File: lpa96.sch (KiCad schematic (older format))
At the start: 26 parts, among them IC1 ATMEGA328-A, P1 CONN_2, P2 CONN_3X2, SW1 SW_PUSH, U1 SD_CARD, U2 LD1117S33, Y1 RESONATEUR

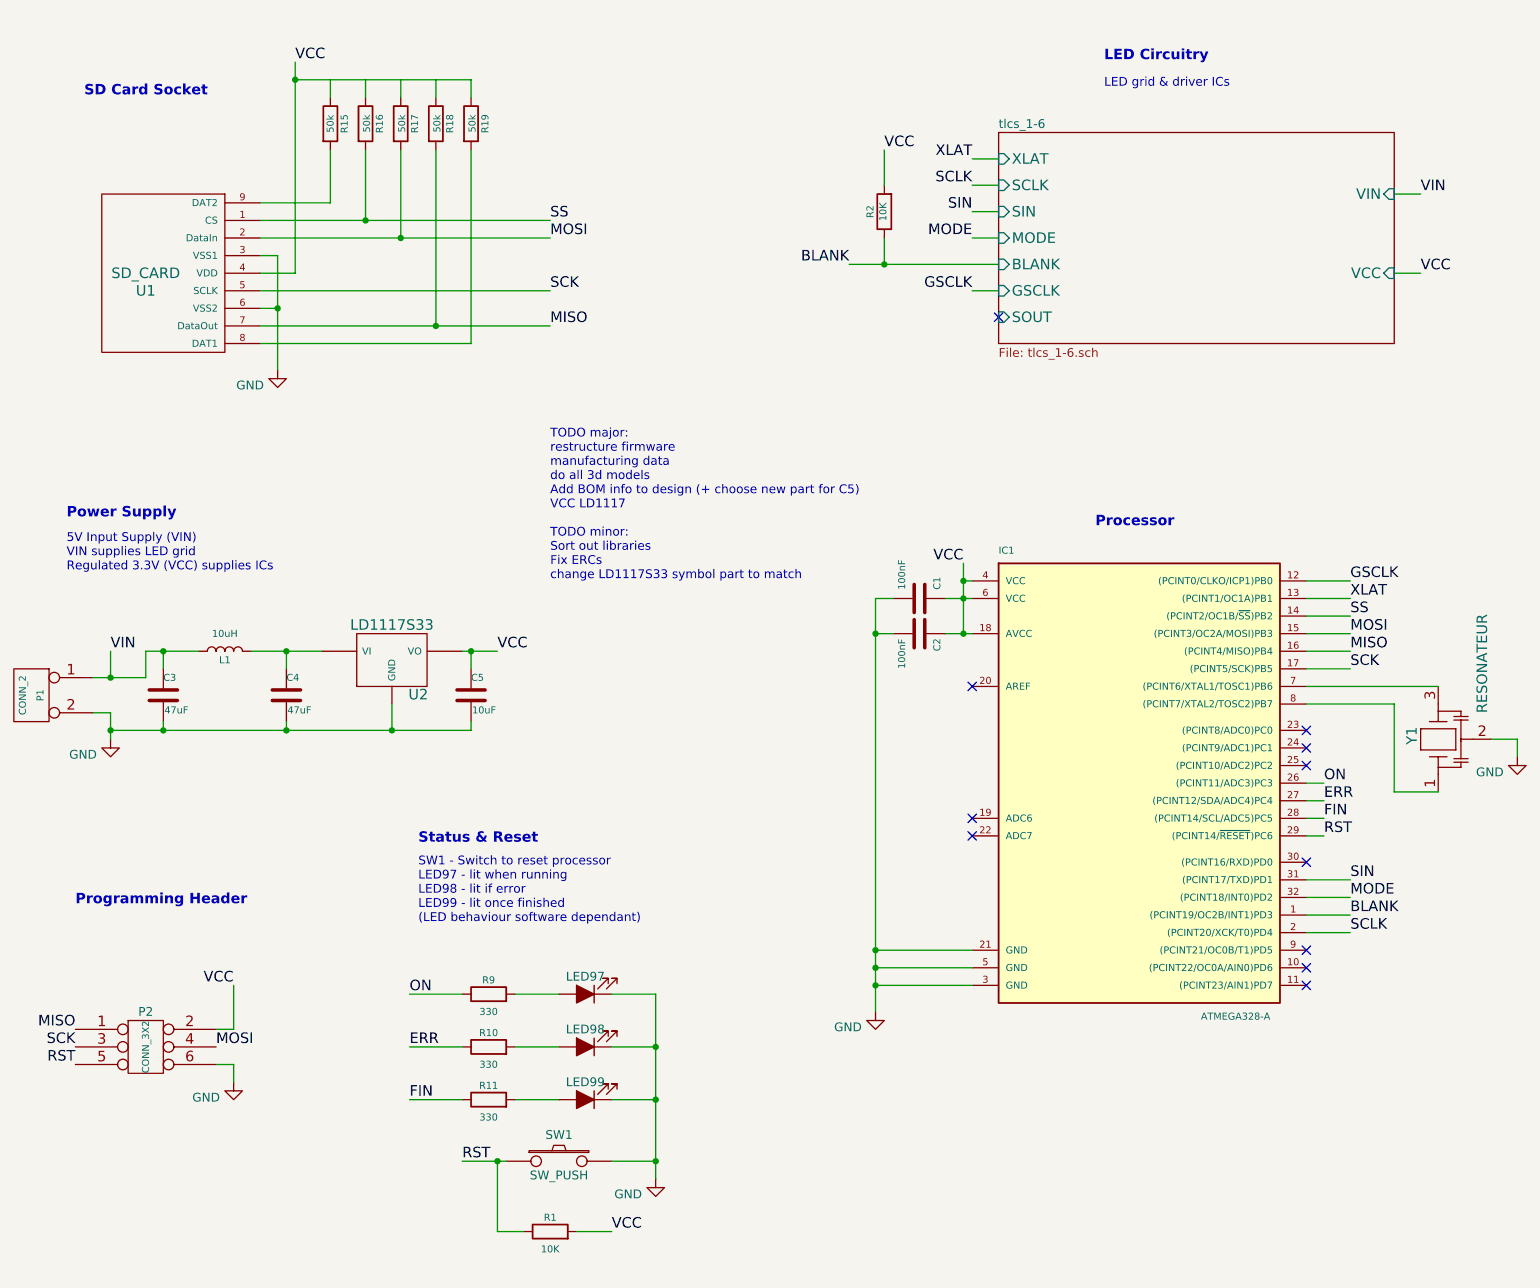
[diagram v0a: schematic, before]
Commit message: renamed project, programming header move and added 3d model
added 3d model for programming header P2
moved P2 away from hole
renamed all files from tca to lpa96 as agreed
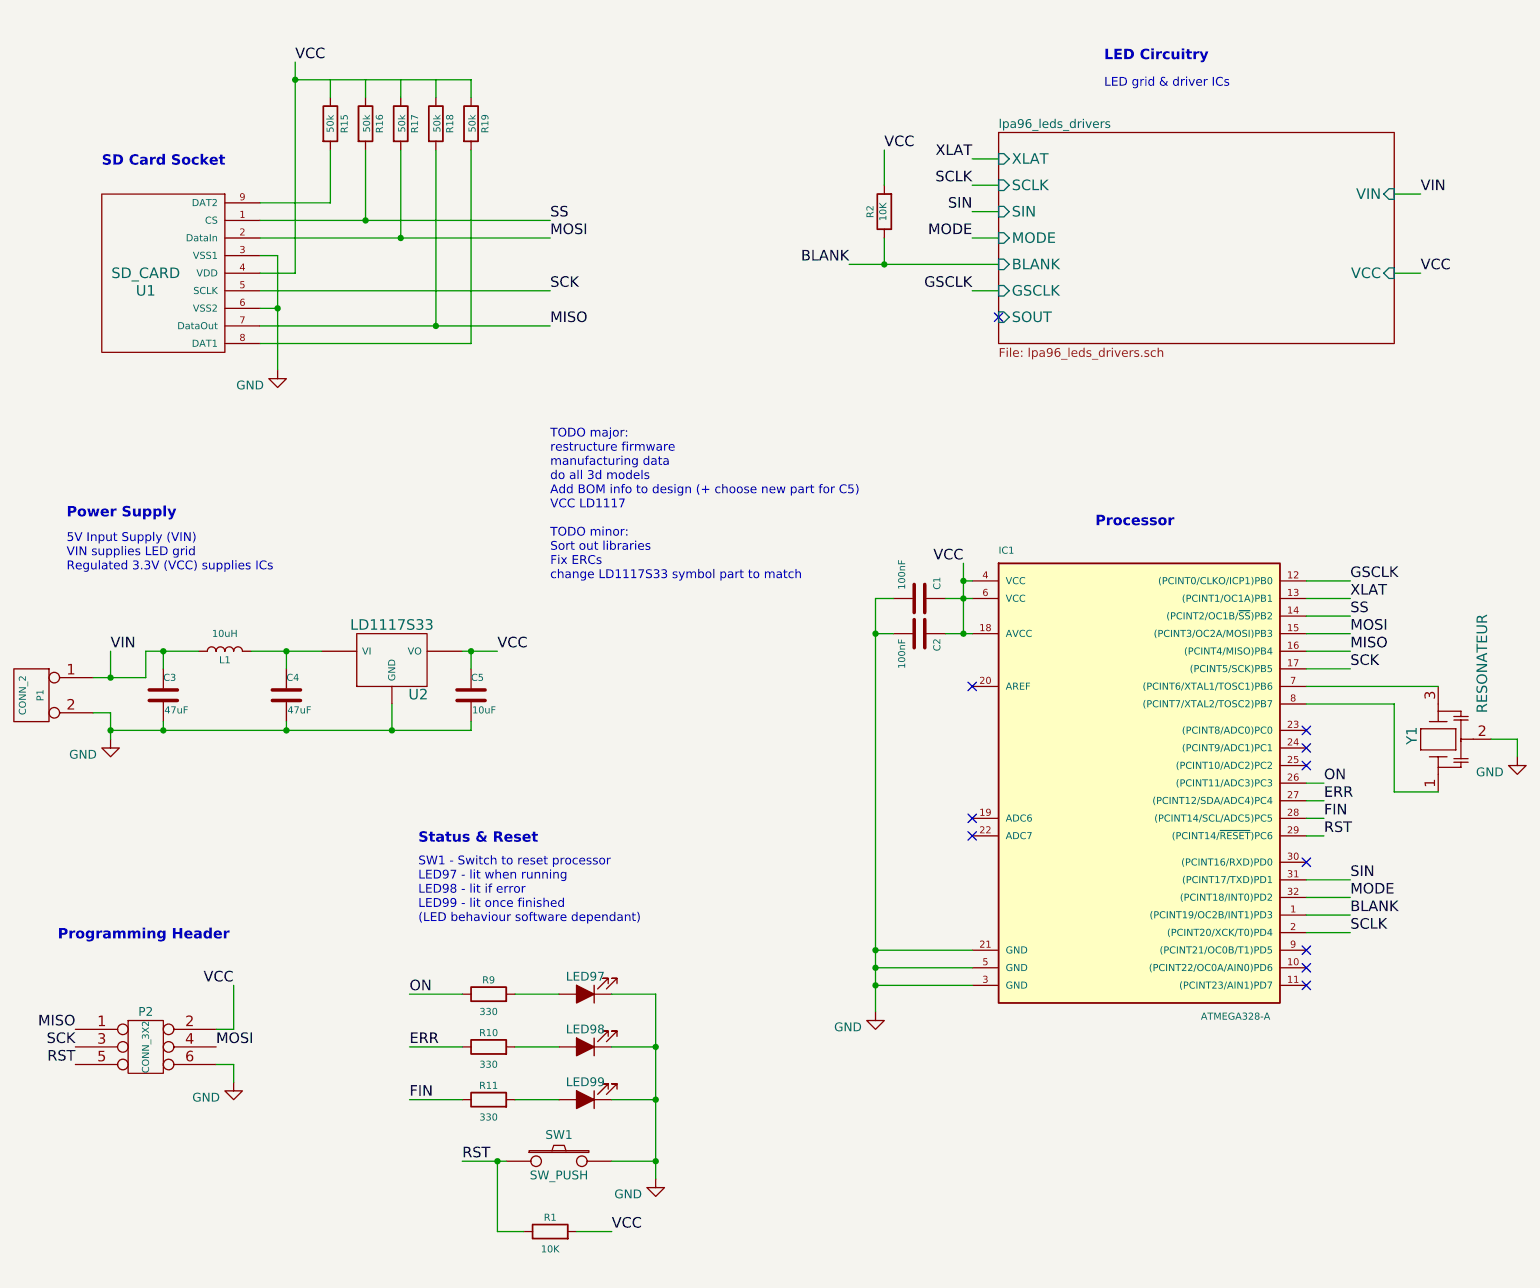
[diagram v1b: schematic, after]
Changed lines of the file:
@@
 EESchema Schematic File Version 4
-LIBS:tca-cache
+LIBS:lpa96-cache
 EELAYER 30 0
 EELAYER END
@@
 S 6950 1300 2250 1200
 U 5362FF20
-F0 "tlcs_1-6" 50
-F1 "tlcs_1-6.sch" 50
+F0 "lpa96_leds_drivers" 50
+F1 "lpa96_leds_drivers.sch" 50
 F2 "XLAT" I L 6950 1450 60
 F3 "SCLK" I L 6950 1600 60
@@
 	3750 2400 4400 2400
 NoConn ~ 6950 2350
-Text Notes 1700 5700 0    59   ~ 12
+Text Notes 1600 5900 0    59   ~ 12
 Programming Header
 Text Notes 1650 3500 0    59   ~ 12
@@
 Text Notes 1650 3800 0    50   ~ 0
 5V Input Supply (VIN)\nVIN supplies LED grid\nRegulated 3.3V (VCC) supplies ICs
-Text Notes 1750 1100 0    59   ~ 12
+Text Notes 1850 1500 0    59   ~ 12
 SD Card Socket
 Text Notes 7550 900  0    59   ~ 12

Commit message: fix ERC errors, added last 3d model, other misc
changed TLC5941 pin29 pad to 'passive' type to fix ERC error
added PWR_FLAG special symbol on to input GND to fix ERC error
changed all VCC to proper power symbol instead of net alias
connected shield tabs of SDCARD footprint to GND (symbol doesn't have a pin)
changed SD_CARD symbol for pin8/9 are passive instead of NC (avoids ERCs)
changed name of pin8/9 from "RSV" to DAT1/DAT2 to match datasheet of guessed part
changed pin4 of regulator back to VCC (got messed up after change to VCC power symbols instead of net alias
added 3d model to P1 (revise after BOM received)
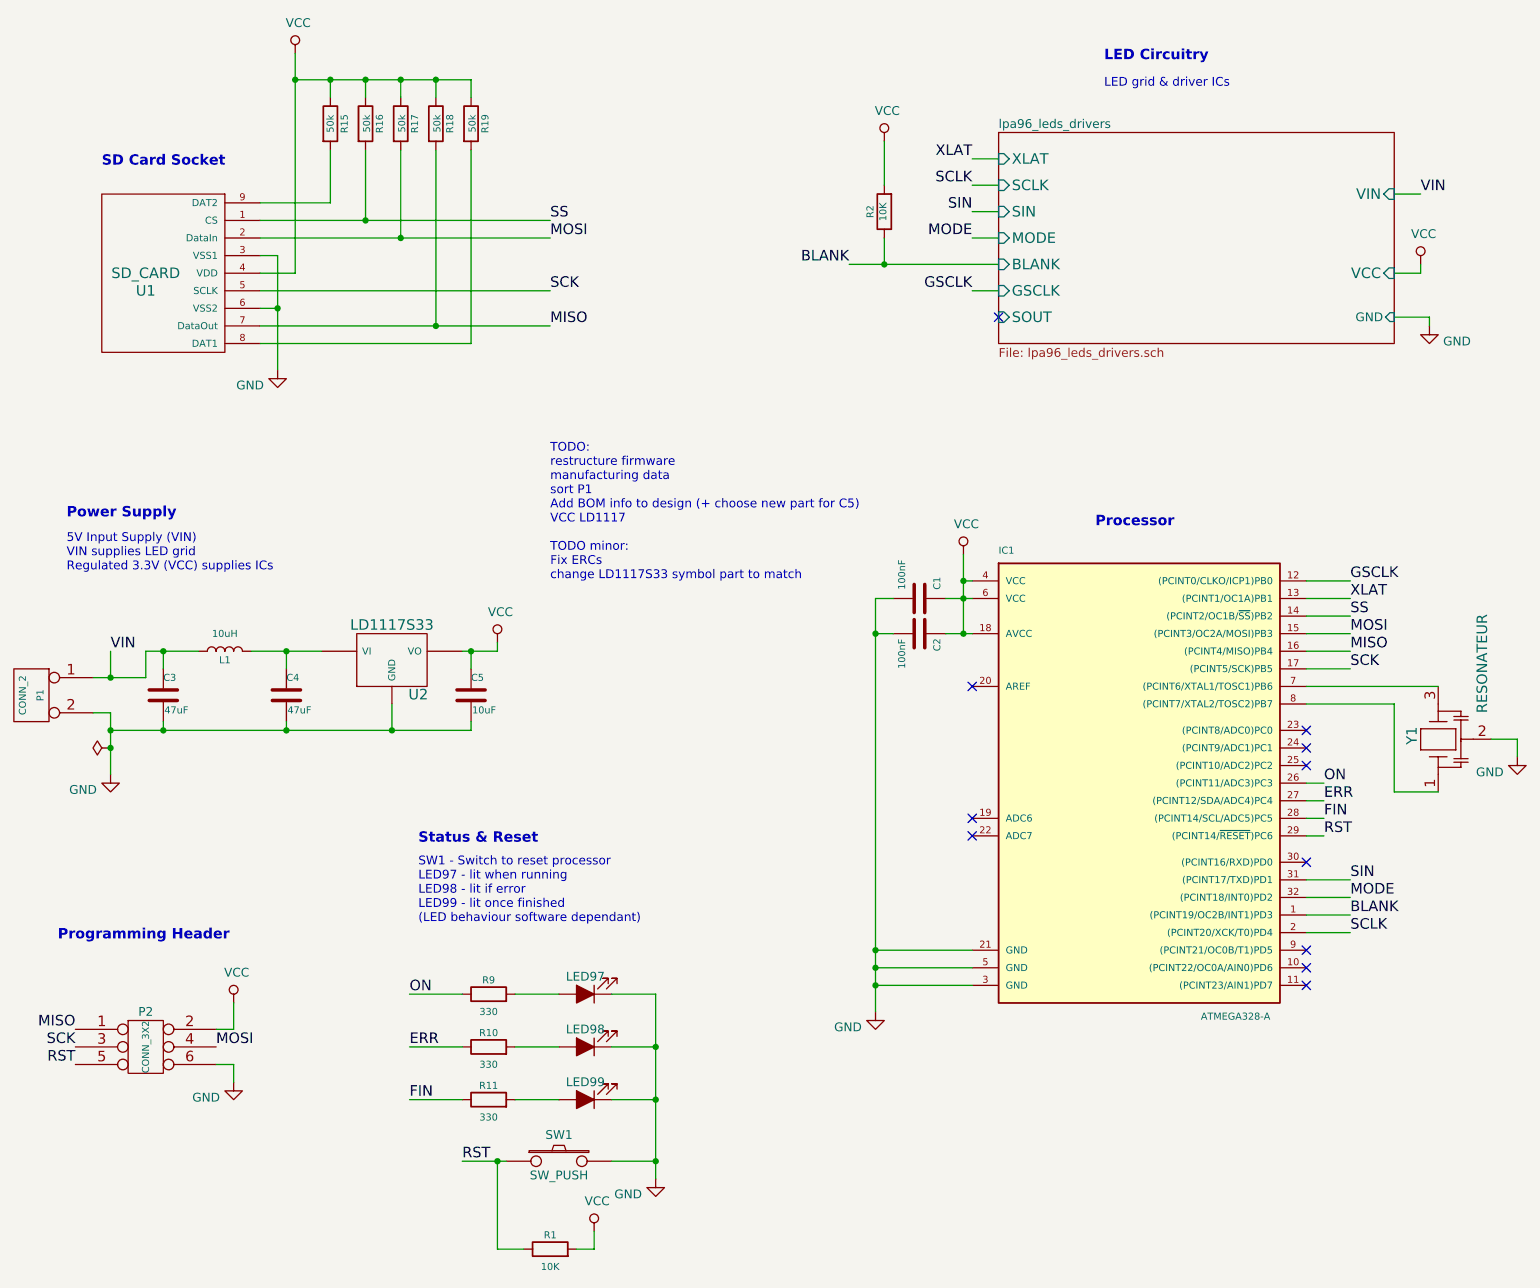
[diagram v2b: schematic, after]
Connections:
- wire segments 123 -> 133
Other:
- note added: "TODO:\nrestructure firmware\nmanufacturing data\nsort P1\nAdd BOM info to design (+ choose new part for C5)\nVCC LD1117\n\nTODO minor:\nFix ERCs\nchange LD1117S33 symbol part to match"
- note removed: "TODO major:\nrestructure firmware\nmanufacturing data\ndo all 3d models\nAdd BOM info to design (+ choose new part for C5)\nVCC LD1117\n\nTODO minor:\nSort out libraries\nFix ERCs\nchange LD1117S33 symbol part to match"
- moved on the sheet: R1
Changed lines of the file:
@@
 Text Label 8950 4050 0    60   ~ 0
 SS
-Text Label 2950 900  0    60   ~ 0
-VCC
 Text Label 4400 2400 0    60   ~ 0
 MISO
@@
 Text Label 8800 5300 0    60   ~ 0
 RST
-Text Label 4750 7550 0    60   ~ 0
-VCC
 NoConn ~ 8700 4700
 NoConn ~ 8700 4800
@@
 Text Label 8950 3950 0    60   ~ 0
 XLAT
-Text Label 6750 3750 2    60   ~ 0
-VCC
 NoConn ~ 6800 4450
 $Comp
@@
 L Device:R R1
 U 1 1 5214E00C
-P 4400 7550
-F 0 "R1" V 4480 7550 40  0000 C CNN
-F 1 "10K" V 4300 7550 40  0000 C CNN
-F 2 "Resistors_SMD:R_0805" V 4330 7550 30  0001 C CNN
-F 3 "~" H 4400 7550 30  0000 C CNN
-	1    4400 7550
+P 4400 7650
+F 0 "R1" V 4480 7650 40  0000 C CNN
+F 1 "10K" V 4300 7650 40  0000 C CNN
+F 2 "Resistors_SMD:R_0805" V 4330 7650 30  0001 C CNN
+F 3 "~" H 4400 7650 30  0000 C CNN
+	1    4400 7650
 	0    -1   -1   0
 $EndComp
 Text Label 8950 4250 0    60   ~ 0
 MISO
-Text Label 2600 6150 2    60   ~ 0
-VCC
 Text Label 2500 6500 0    60   ~ 0
 MOSI
@@
 Text Label 1700 6400 2    60   ~ 0
 MISO
-Text Label 4100 4250 0    60   ~ 0
-VCC
 $Comp
 L lpa96_symbols:CONN_2 P1
@@
 	1    0    0    -1
 $EndComp
-$Sheet
-S 6950 1300 2250 1200
-U 5362FF20
-F0 "lpa96_leds_drivers" 50
-F1 "lpa96_leds_drivers.sch" 50
-F2 "XLAT" I L 6950 1450 60
-F3 "SCLK" I L 6950 1600 60
-F4 "SIN" I L 6950 1750 60
-F5 "MODE" I L 6950 1900 60
-F6 "BLANK" I L 6950 2050 60
-F7 "GSCLK" I L 6950 2200 60
-F8 "VIN" I R 9200 1650 60
-F9 "VCC" I R 9200 2100 60
-F10 "SOUT" I L 6950 2350 60
-$EndSheet
 $Comp
 L Device:R R2
@@
 	-1   0    0    1
 $EndComp
-Text Label 6300 1400 0    60   ~ 0
-VCC
 Text Label 6800 1450 2    60   ~ 0
 XLAT
@@
 Text Label 9350 1650 0    60   ~ 0
 VIN
-Text Label 9350 2100 0    60   ~ 0
-VCC
 Text Label 6100 2050 2    60   ~ 0
 BLANK
@@
 	1800 4400 1900 4400
 Connection ~ 4100 7150
-Wire Wire Line
-	4100 7550 4100 7150
 Connection ~ 5000 7150
 Wire Wire Line
@@
 Connection ~ 6750 3950
 Wire Wire Line
-	6750 3750 6750 3850
-Wire Wire Line
 	6800 3850 6750 3850
 Wire Wire Line
@@
 	2500 6600 2600 6600
 Wire Wire Line
-	2600 6400 2600 6150
-Wire Wire Line
 	2500 6400 2600 6400
 Wire Wire Line
@@
 Wire Wire Line
 	9200 1650 9350 1650
-Wire Wire Line
-	9200 2100 9350 2100
 Connection ~ 6300 2050
 Connection ~ 2900 4250
 Wire Wire Line
 	2850 2000 2850 2300
-Connection ~ 2850 2300
 Wire Wire Line
 	2850 2000 2750 2000
@@
 	3150 1700 2750 1700
 Wire Wire Line
-	2950 900  2950 1000
-Wire Wire Line
 	2950 2100 2750 2100
 Connection ~ 3350 1800
@@
 	6250 6050 6250 6150
 Wire Wire Line
-	1900 4700 1900 4750
-Wire Wire Line
 	1900 4400 2100 4400
 Wire Wire Line
@@
 Wire Wire Line
 	2900 4250 3100 4250
-Wire Wire Line
-	2850 2300 2850 2650
 Wire Wire Line
 	2950 1000 2950 2100
@@
 SW1 - Switch to reset processor\nLED97 - lit when running\nLED98 - lit if error\nLED99 - lit once finished\n(LED behaviour software dependant)
 Text Notes 4400 3850 0    50   ~ 0
-TODO major:\nrestructure firmware\nmanufacturing data\ndo all 3d models\nAdd BOM info to design (+ choose new part for C5)\nVCC LD1117\n\nTODO minor:\nSort out libraries\nFix ERCs\nchange LD1117S33 symbol part to match
+TODO:\nrestructure firmware\nmanufacturing data\nsort P1\nAdd BOM info to design (+ choose new part for C5)\nVCC LD1117\n\nTODO minor:\nFix ERCs\nchange LD1117S33 symbol part to match
 Wire Wire Line
 	3950 4250 4100 4250
@@
 L power:GND #PWR?
 U 1 1 5D684D23
-P 1900 4750
+P 1900 4950
 AR Path="/5362FF20/5D684D23" Ref="#PWR?"  Part="1"
 AR Path="/5D684D23" Ref="#PWR0112"  Part="1"
-F 0 "#PWR0112" H 1900 4500 50  0001 C CNN
-F 1 "GND" H 1822 4633 50  0000 R BNN
-F 2 "" H 1900 4750 50  0001 C CNN
-F 3 "" H 1900 4750 50  0001 C CNN
-	1    1900 4750
+F 0 "#PWR0112" H 1900 4700 50  0001 C CNN
+F 1 "GND" H 1822 4833 50  0000 R BNN
+F 2 "" H 1900 4950 50  0001 C CNN
+F 3 "" H 1900 4950 50  0001 C CNN
+	1    1900 4950
 	1    0    0    -1
 $EndComp
@@
 $EndComp
 Wire Wire Line
-	6300 1400 6300 1600
-Wire Wire Line
 	6300 1900 6300 2050
 Wire Wire Line
-	2950 1000 3950 1000
-Wire Wire Line
-	3150 1000 3150 1100
+	2950 1000 3150 1000
 Wire Wire Line
 	3150 1400 3150 1700
 Wire Wire Line
-	3350 1000 3350 1100
-Wire Wire Line
 	3350 1400 3350 1800
 Wire Wire Line
-	3550 1000 3550 1100
-Wire Wire Line
 	3550 1400 3550 1900
 Wire Wire Line
-	3750 1000 3750 1100
-Wire Wire Line
 	3750 1400 3750 2400
 Wire Wire Line
@@
 Wire Wire Line
 	4200 6800 4450 6800
-Wire Wire Line
-	4550 7550 4750 7550
-Wire Wire Line
-	4100 7550 4250 7550
 Connection ~ 3500 4700
 Text Notes 3650 5350 0    59   ~ 12
@@
 Wire Wire Line
 	6650 3950 6750 3950
+Wire Wire Line
+	3750 1100 3750 1000
+Connection ~ 3750 1000
+Wire Wire Line
+	3750 1000 3950 1000
+Wire Wire Line
+	3550 1100 3550 1000
+Connection ~ 3550 1000
+Wire Wire Line
+	3550 1000 3750 1000
+Wire Wire Line
+	3350 1100 3350 1000
+Connection ~ 3350 1000
+Wire Wire Line
+	3350 1000 3550 1000
+Wire Wire Line
+	3150 1100 3150 1000
+Connection ~ 3150 1000
+Wire Wire Line
+	3150 1000 3350 1000
+Wire Wire Line
+	2850 2300 2850 2650
+Connection ~ 2850 2300
+$Comp
+L power:GND #PWR?
+U 1 1 5D79002C
+P 9400 2400
+AR Path="/5362FF20/5D79002C" Ref="#PWR?"  Part="1"
+AR Path="/5D79002C" Ref="#PWR0102"  Part="1"
+F 0 "#PWR0102" H 9400 2150 50  0001 C CNN
+F 1 "GND" H 9322 2283 50  0000 R BNN
+F 2 "" H 9400 2400 50  0001 C CNN
+F 3 "" H 9400 2400 50  0001 C CNN
+	1    9400 2400
+	-1   0    0    -1
+$EndComp
+Wire Wire Line
+	9400 2400 9400 2350
+Wire Wire Line
+	9400 2350 9200 2350
+$Comp
+L power:VCC #PWR0120
+U 1 1 5D7E76B2
+P 4100 4200
+F 0 "#PWR0120" H 4100 4050 50  0001 C CNN
+F 1 "VCC" H 4117 4373 50  0000 C CNN
+F 2 "" H 4100 4200 50  0001 C CNN
+F 3 "" H 4100 4200 50  0001 C CNN
+	1    4100 4200
+	1    0    0    -1
+$EndComp
+Wire Wire Line
+	4100 4250 4100 4200
+$Comp
+L power:VCC #PWR0121
+U 1 1 5DBB9CE0
+P 2950 850
+F 0 "#PWR0121" H 2950 700 50  0001 C CNN
+F 1 "VCC" H 2967 1023 50  0000 C CNN
+F 2 "" H 2950 850 50  0001 C CNN
+F 3 "" H 2950 850 50  0001 C CNN
+	1    2950 850
+	1    0    0    -1
+$EndComp
+Wire Wire Line
+	2950 850  2950 1000
+$Comp
+L power:VCC #PWR0122
+U 1 1 5DBBF76D
+P 6300 1350
+F 0 "#PWR0122" H 6300 1200 50  0001 C CNN
+F 1 "VCC" H 6317 1523 50  0000 C CNN
+F 2 "" H 6300 1350 50  0001 C CNN
+F 3 "" H 6300 1350 50  0001 C CNN
+	1    6300 1350
+	1    0    0    -1
+$EndComp
+Wire Wire Line
+	6300 1350 6300 1600
+Wire Wire Line
+	9200 2100 9350 2100
+$Comp
+L power:VCC #PWR0123
+U 1 1 5DBC5311
+P 9350 2050
+F 0 "#PWR0123" H 9350 1900 50  0001 C CNN
+F 1 "VCC" H 9367 2223 50  0000 C CNN
+F 2 "" H 9350 2050 50  0001 C CNN
+F 3 "" H 9350 2050 50  0001 C CNN
+	1    9350 2050
+	1    0    0    -1
+$EndComp
+Wire Wire Line
+	9350 2100 9350 2050
+$Comp
+L power:VCC #PWR0124
+U 1 1 5DBCAA86
+P 6750 3700
+F 0 "#PWR0124" H 6750 3550 50  0001 C CNN
+F 1 "VCC" H 6767 3873 50  0000 C CNN
+F 2 "" H 6750 3700 50  0001 C CNN
+F 3 "" H 6750 3700 50  0001 C CNN
+	1    6750 3700
+	1    0    0    -1
+$EndComp
+Wire Wire Line
+	6750 3700 6750 3850
+$Comp
+L power:VCC #PWR0125
+U 1 1 5DBD5D00
+P 2600 6250
+F 0 "#PWR0125" H 2600 6100 50  0001 C CNN
+F 1 "VCC" H 2617 6423 50  0000 C CNN
+F 2 "" H 2600 6250 50  0001 C CNN
+F 3 "" H 2600 6250 50  0001 C CNN
+	1    2600 6250
+	1    0    0    -1
+$EndComp
+Wire Wire Line
+	2600 6250 2600 6400
+$Sheet
+S 6950 1300 2250 1200
+U 5362FF20
+F0 "lpa96_leds_drivers" 50
+F1 "lpa96_leds_drivers.sch" 50
+F2 "XLAT" I L 6950 1450 60
+F3 "SCLK" I L 6950 1600 60
+F4 "SIN" I L 6950 1750 60
+F5 "MODE" I L 6950 1900 60
+F6 "BLANK" I L 6950 2050 60
+F7 "GSCLK" I L 6950 2200 60
+F8 "VIN" I R 9200 1650 60
+F9 "VCC" I R 9200 2100 60
+F10 "SOUT" I L 6950 2350 60
+F11 "GND" I R 9200 2350 50
+$EndSheet
+$Comp
+L power:VCC #PWR0133
+U 1 1 5DC377B0
+P 4650 7550
+F 0 "#PWR0133" H 4650 7400 50  0001 C CNN
+F 1 "VCC" H 4667 7723 50  0000 C CNN
+F 2 "" H 4650 7550 50  0001 C CNN
+F 3 "" H 4650 7550 50  0001 C CNN
+	1    4650 7550
+	1    0    0    -1
+$EndComp
+Wire Wire Line
+	4650 7650 4550 7650
+Wire Wire Line
+	4650 7550 4650 7650
+Wire Wire Line
+	4250 7650 4100 7650
+Wire Wire Line
+	4100 7150 4100 7650
+$Comp
+L power:PWR_FLAG #FLG0101
+U 1 1 5DC82CA6
+P 1900 4800
+F 0 "#FLG0101" H 1900 4875 50  0001 C CNN
+F 1 "PWR_FLAG" V 1900 5100 50  0001 C CNN
+F 2 "" H 1900 4800 50  0001 C CNN
+F 3 "~" H 1900 4800 50  0001 C CNN
+	1    1900 4800
+	0    -1   -1   0
+$EndComp
+Wire Wire Line
+	1900 4700 1900 4800
+Connection ~ 1900 4800
+Wire Wire Line
+	1900 4800 1900 4950
 $EndSCHEMATC
